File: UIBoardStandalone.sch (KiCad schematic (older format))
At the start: 61 parts, among them J1 Conn_02x08_Odd_Even, J2 Conn_02x15_Odd_Even, SW1 Button_X, SW10 Button_6, SW11 Button_S, SW12 Button_7, SW13 Button_8, SW14 Button_9, SW15 Button_G, SW16 Button_Y, SW17 Button_0, SW18 Button_Z, SW2 Button_R, SW3 Button_1, SW4 Button_2, SW5 Button_3, SW6 Button_P, SW7 Button_M, SW8 Button_4, SW9 Button_5, U1 HD1077R, U10 HD1077R, U11 HD1077R, U12 HD1077R, U13 HD1077R, U14 HD1077R, U15 HD1077R, U16 HD1077R, U17 MM74C923WM, U2 HD1077R, U3 HD1077R, U4 HD1077R, U5 HD1077R, U6 HD1077R, U7 HD1077R, U8 HD1077R, U9 HD1077R

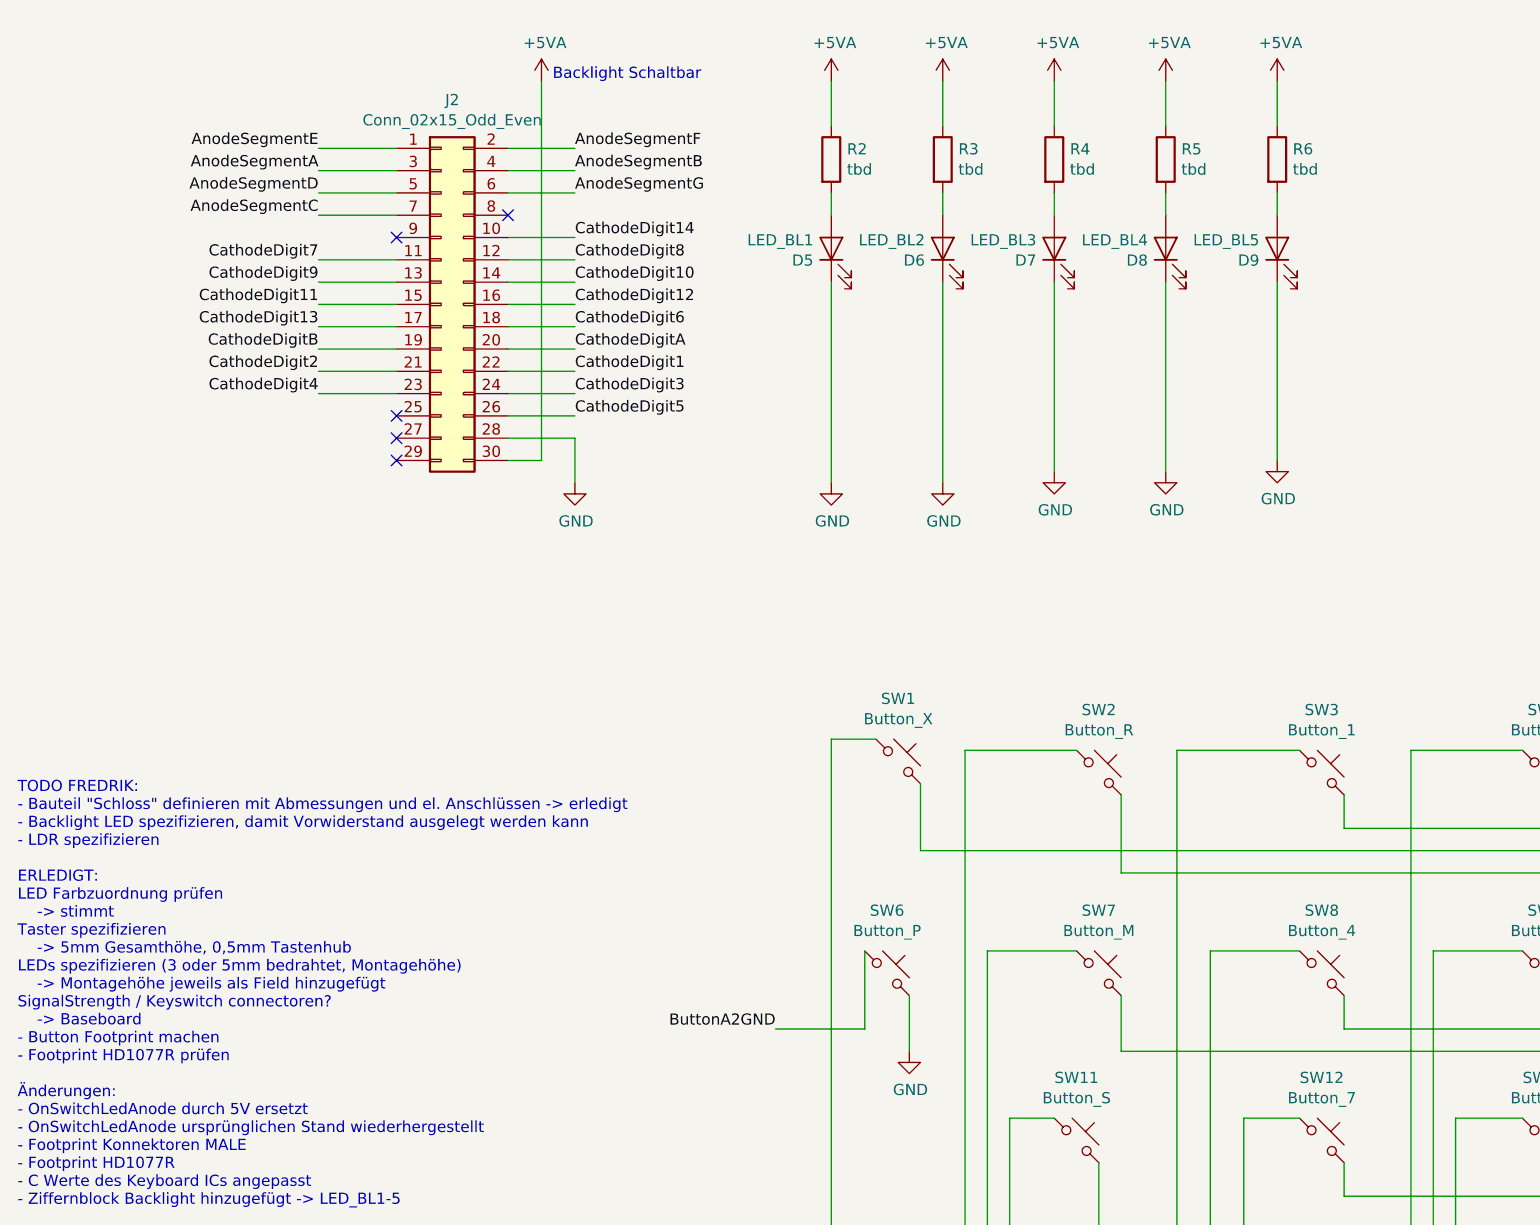
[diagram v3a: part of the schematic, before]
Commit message: - R Values hinzugefügt - Text aktualisiert - vorläufe BOM hinzugefügt
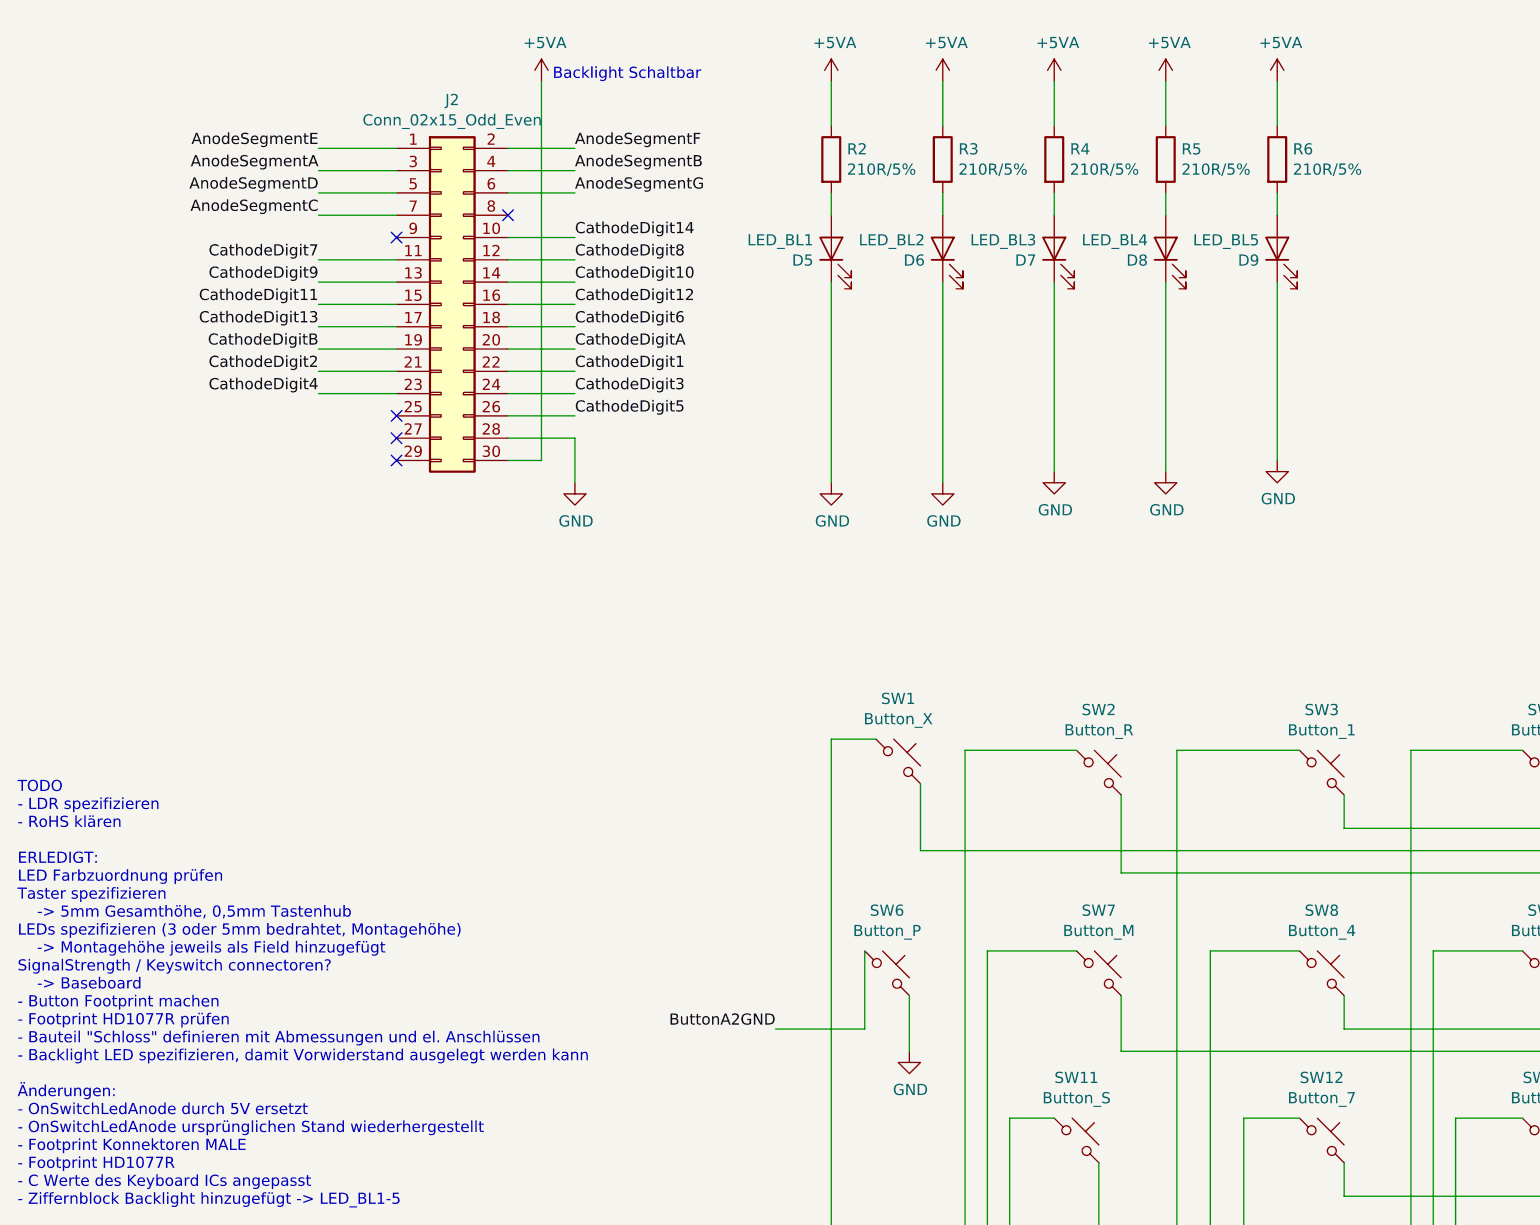
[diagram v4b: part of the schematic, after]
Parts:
- D1, D2, D3: Montagehoehe Lichtes Mass (none) -> 9mm; Montagehöhe 9mm -> (none)
- D4: Montagehoehe Lichtes Mass (none) -> 8mm; Montagehöhe 8mm -> (none)
- D5, D6, D7, D8, D9: Digikey Part Number 1516-QBL7IW60D-WW-ND -> (none); Montagehoehe Lichtes Mass (none) -> 10mm; Montagehöhe 10mm -> (none)
- R1: Montagehoehe Lichtes Mass (none) -> 7mm; Montagehöhe 7mm -> (none)
- R2, R3, R4, R5, R6: value tbd -> 210R/5%
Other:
- note added: "TODO\n- LDR spezifizieren\n- RoHS klären\n\nERLEDIGT:\nLED Farbzuordnung prüfen\nTaster spezifizieren\n -> 5mm Gesamthöhe, 0,5mm Tastenhub\nLEDs spezifizieren (3 oder 5mm bedrahtet, Montagehöhe)\n -> Montagehöhe jeweils als Field hinzugefügt\nSignalStrength / Keyswitch connectoren?\n -> Baseboard\n- Button Footprint machen\n- Footprint HD1077R prüfen\n- Bauteil "Schloss" definieren mit Abmessunge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"
- note removed: "TODO FREDRIK:\n- Bauteil "Schloss" definieren mit Abmessungen und el. Anschlüssen -> erledigt\n- Backlight LED spezifizieren, damit Vorwiderstand ausgelegt werden kann\n- LDR spezifizieren\n\nERLEDIGT:\nLED Farbzuordnung prüfen\n -> stimmt\nTaster spezifizieren\n -> 5mm Gesamthöhe, 0,5mm Tastenhub\nLEDs spezifizieren (3 oder 5mm bedrahtet, Montagehöhe)\n -> Montagehöhe jeweils als Field hinzugefü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"
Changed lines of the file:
@@
 F 1 "LED_RD" V 10788 4330 50  0000 L CNN
 F 2 "LED_THT:LED_D5.0mm" H 10750 4250 50  0001 C CNN
-F 3 "https://www.aopled.com/AOP_PDFs/L513SRD-B.pdf" H 10750 4250 50  0001 C CNN
-F 4 "9mm" V 10750 4250 50  0001 C CNN "Montagehöhe"
+F 3 "" H 10750 4250 50  0001 C CNN
+F 4 "9mm" V 10750 4250 50  0001 C CNN "Montagehoehe Lichtes Mass"
 	1    10750 4250
 	0    -1   -1   0
@@
 F 1 "LED_YL" V 10288 4330 50  0000 L CNN
 F 2 "LED_THT:LED_D5.0mm" H 10250 4250 50  0001 C CNN
-F 3 "https://media.digikey.com/pdf/Data%20Sheets/Lite-On%20PDFs/LTL-4273.pdf" H 10250 4250 50  0001 C CNN
-F 4 "9mm" V 10250 4250 50  0001 C CNN "Montagehöhe"
+F 3 "" H 10250 4250 50  0001 C CNN
+F 4 "9mm" V 10250 4250 50  0001 C CNN "Montagehoehe Lichtes Mass"
 	1    10250 4250
 	0    -1   -1   0
@@
 F 1 "LED_GN" V 9638 4330 50  0000 L CNN
 F 2 "LED_THT:LED_D5.0mm" H 9600 4250 50  0001 C CNN
-F 3 "https://www.aopled.com/AOP_PDFs/L513GD-B.pdf" H 9600 4250 50  0001 C CNN
-F 4 "9mm" V 9600 4250 50  0001 C CNN "Montagehöhe"
+F 3 "" H 9600 4250 50  0001 C CNN
+F 4 "9mm" V 9600 4250 50  0001 C CNN "Montagehoehe Lichtes Mass"
 	1    9600 4250
 	0    -1   -1   0
@@
 F 1 "LED_ON" V 11288 4330 50  0000 L CNN
 F 2 "LED_THT:LED_D3.0mm" H 11250 4250 50  0001 C CNN
-F 3 "https://media.digikey.com/pdf/Data%20Sheets/Lite-On%20PDFs/LTL-1CHYE.pdf" H 11250 4250 50  0001 C CNN
-F 4 "8mm" V 11250 4250 50  0001 C CNN "Montagehöhe"
+F 3 "" H 11250 4250 50  0001 C CNN
+F 4 "8mm" V 11250 4250 50  0001 C CNN "Montagehoehe Lichtes Mass"
 	1    11250 4250
 	0    -1   -1   0
@@
 F 1 "LDR" H 11970 4255 50  0000 L CNN
 F 2 "OptoDevice:R_LDR_4.9x4.2mm_P2.54mm_Vertical" V 11950 4050 50  0001 L CNN
-F 3 "~" H 11900 4250 50  0001 C CNN
-F 4 "7mm" H 11900 4300 50  0001 C CNN "Montagehöhe"
+F 3 "" H 11900 4250 50  0001 C CNN
+F 4 "7mm" H 11900 4300 50  0001 C CNN "Montagehoehe Lichtes Mass"
 	1    11900 4300
 	-1   0    0    1
@@
 LED_GN
 Text Notes 1050 8550 0    50   ~ 0
-TODO FREDRIK:\n- Bauteil "Schloss" definieren mit Abmessungen und el. Anschlüssen -> erledigt\n- Backlight LED spezifizieren, damit Vorwiderstand ausgelegt werden kann\n- LDR spezifizieren\n\nERLEDIGT:\nLED Farbzuordnung prüfen\n    -> stimmt\nTaster spezifizieren\n    -> 5mm Gesamthöhe, 0,5mm Tastenhub\nLEDs spezifizieren (3 oder 5mm bedrahtet, Montagehöhe)\n    -> Montagehöhe jeweils als Field hinzugefügt\nSignalStrength / Keyswitch connectoren?\n    -> Baseboard\n- Button Footprint machen\n- Footprint HD1077R prüfen\n\nÄnderungen:\n- OnSwitchLedAnode durch 5V ersetzt\n- OnSwitchLedAnode ursprünglichen Stand wiederhergestellt\n- Footprint Konnektoren MALE\n- Footprint HD1077R\n- C Werte des Keyboard ICs angepasst\n- Ziffernblock Backlight hinzugefügt -> LED_BL1-5
+TODO\n- LDR spezifizieren\n- RoHS klären\n\nERLEDIGT:\nLED Farbzuordnung prüfen\nTaster spezifizieren\n    -> 5mm Gesamthöhe, 0,5mm Tastenhub\nLEDs spezifizieren (3 oder 5mm bedrahtet, Montagehöhe)\n    -> Montagehöhe jeweils als Field hinzugefügt\nSignalStrength / Keyswitch connectoren?\n    -> Baseboard\n- Button Footprint machen\n- Footprint HD1077R prüfen\n- Bauteil "Schloss" definieren mit Abmessungen und el. Anschlüssen\n- Backlight LED spezifizieren, damit Vorwiderstand ausgelegt werden kann\n\nÄnderungen:\n- OnSwitchLedAnode durch 5V ersetzt\n- OnSwitchLedAnode ursprünglichen Stand wiederhergestellt\n- Footprint Konnektoren MALE\n- Footprint HD1077R\n- C Werte des Keyboard ICs angepasst\n- Ziffernblock Backlight hinzugefügt -> LED_BL1-5
 Wire Wire Line
 	13650 4700 13900 4700
@@
 F 1 "LED_BL1" V 4738 4330 50  0000 L CNN
 F 2 "LED_THT:LED_D3.0mm" H 4700 4250 50  0001 C CNN
-F 3 "http://www.qt-brightek.com/datasheet/QBL7IW60D-XX.pdf" H 4700 4250 50  0001 C CNN
-F 4 "10mm" V 4700 4250 50  0001 C CNN "Montagehöhe"
-F 5 "1516-QBL7IW60D-WW-ND" V 4700 4250 50  0001 C CNN "Digikey Part Number"
+F 3 "" H 4700 4250 50  0001 C CNN
+F 4 "10mm" V 4700 4250 50  0001 C CNN "Montagehoehe Lichtes Mass"
 	1    4700 4250
 	0    -1   -1   0
@@
 F 1 "LED_BL2" V 5238 4330 50  0000 L CNN
 F 2 "LED_THT:LED_D3.0mm" H 5200 4250 50  0001 C CNN
-F 3 "http://www.qt-brightek.com/datasheet/QBL7IW60D-XX.pdf" H 5200 4250 50  0001 C CNN
-F 4 "10mm" V 5200 4250 50  0001 C CNN "Montagehöhe"
-F 5 "1516-QBL7IW60D-WW-ND" V 5200 4250 50  0001 C CNN "Digikey Part Number"
+F 3 "" H 5200 4250 50  0001 C CNN
+F 4 "10mm" V 5200 4250 50  0001 C CNN "Montagehoehe Lichtes Mass"
 	1    5200 4250
 	0    -1   -1   0
@@
 F 1 "LED_BL3" V 5738 4330 50  0000 L CNN
 F 2 "LED_THT:LED_D3.0mm" H 5700 4250 50  0001 C CNN
-F 3 "http://www.qt-brightek.com/datasheet/QBL7IW60D-XX.pdf" H 5700 4250 50  0001 C CNN
-F 4 "10mm" V 5700 4250 50  0001 C CNN "Montagehöhe"
-F 5 "1516-QBL7IW60D-WW-ND" V 5700 4250 50  0001 C CNN "Digikey Part Number"
+F 3 "" H 5700 4250 50  0001 C CNN
+F 4 "10mm" V 5700 4250 50  0001 C CNN "Montagehoehe Lichtes Mass"
 	1    5700 4250
 	0    -1   -1   0
@@
 F 1 "LED_BL4" V 6238 4330 50  0000 L CNN
 F 2 "LED_THT:LED_D3.0mm" H 6200 4250 50  0001 C CNN
-F 3 "http://www.qt-brightek.com/datasheet/QBL7IW60D-XX.pdf" H 6200 4250 50  0001 C CNN
-F 4 "10mm" V 6200 4250 50  0001 C CNN "Montagehöhe"
-F 5 "1516-QBL7IW60D-WW-ND" V 6200 4250 50  0001 C CNN "Digikey Part Number"
+F 3 "" H 6200 4250 50  0001 C CNN
+F 4 "10mm" V 6200 4250 50  0001 C CNN "Montagehoehe Lichtes Mass"
 	1    6200 4250
 	0    -1   -1   0
@@
 F 1 "LED_BL5" V 6738 4330 50  0000 L CNN
 F 2 "LED_THT:LED_D3.0mm" H 6700 4250 50  0001 C CNN
-F 3 "http://www.qt-brightek.com/datasheet/QBL7IW60D-XX.pdf" H 6700 4250 50  0001 C CNN
-F 4 "10mm" V 6700 4250 50  0001 C CNN "Montagehöhe"
-F 5 "1516-QBL7IW60D-WW-ND" V 6700 4250 50  0001 C CNN "Digikey Part Number"
+F 3 "" H 6700 4250 50  0001 C CNN
+F 4 "10mm" V 6700 4250 50  0001 C CNN "Montagehoehe Lichtes Mass"
 	1    6700 4250
 	0    -1   -1   0
@@
 P 4700 3850
 F 0 "R2" H 4770 3896 50  0000 L CNN
-F 1 "tbd" H 4770 3805 50  0000 L CNN
+F 1 "210R/5%" H 4770 3805 50  0000 L CNN
 F 2 "Resistor_SMD:R_0603_1608Metric" V 4630 3850 50  0001 C CNN
 F 3 "~" H 4700 3850 50  0001 C CNN
@@
 P 5200 3850
 F 0 "R3" H 5270 3896 50  0000 L CNN
-F 1 "tbd" H 5270 3805 50  0000 L CNN
+F 1 "210R/5%" H 5270 3805 50  0000 L CNN
 F 2 "Resistor_SMD:R_0603_1608Metric" V 5130 3850 50  0001 C CNN
 F 3 "~" H 5200 3850 50  0001 C CNN
@@
 P 5700 3850
 F 0 "R4" H 5770 3896 50  0000 L CNN
-F 1 "tbd" H 5770 3805 50  0000 L CNN
+F 1 "210R/5%" H 5770 3805 50  0000 L CNN
 F 2 "Resistor_SMD:R_0603_1608Metric" V 5630 3850 50  0001 C CNN
 F 3 "~" H 5700 3850 50  0001 C CNN
@@
 P 6200 3850
 F 0 "R5" H 6270 3896 50  0000 L CNN
-F 1 "tbd" H 6270 3805 50  0000 L CNN
+F 1 "210R/5%" H 6270 3805 50  0000 L CNN
 F 2 "Resistor_SMD:R_0603_1608Metric" V 6130 3850 50  0001 C CNN
 F 3 "~" H 6200 3850 50  0001 C CNN
@@
 P 6700 3850
 F 0 "R6" H 6770 3896 50  0000 L CNN
-F 1 "tbd" H 6770 3805 50  0000 L CNN
+F 1 "210R/5%" H 6770 3805 50  0000 L CNN
 F 2 "Resistor_SMD:R_0603_1608Metric" V 6630 3850 50  0001 C CNN
 F 3 "~" H 6700 3850 50  0001 C CNN

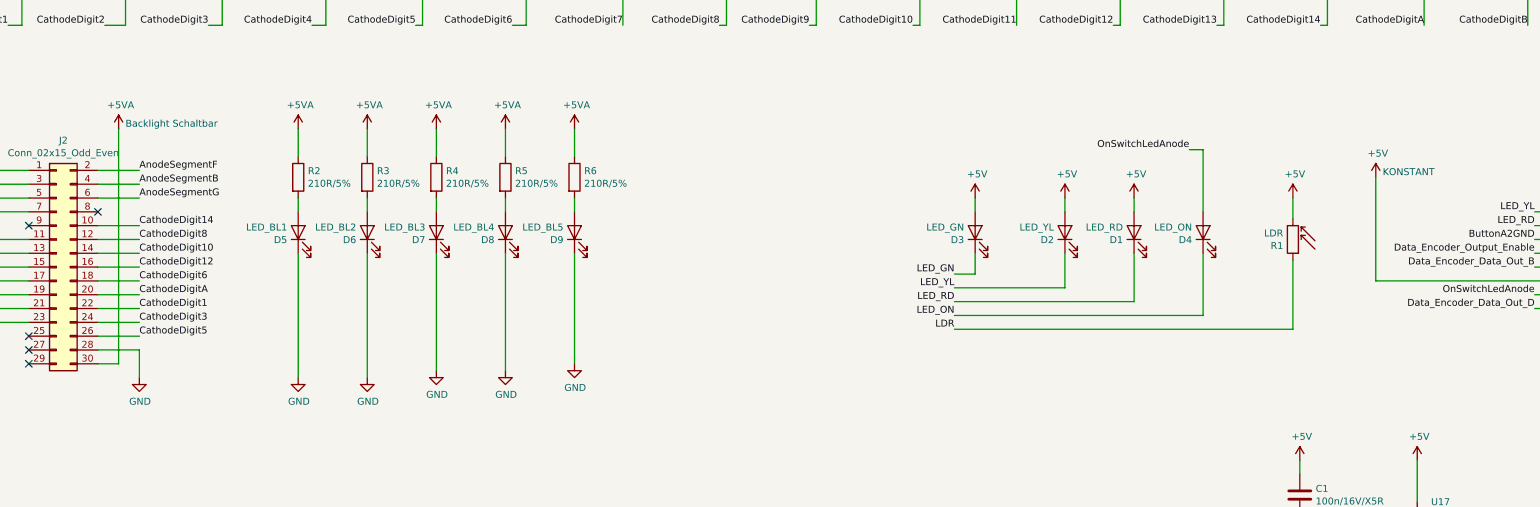
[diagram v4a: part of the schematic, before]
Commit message: - UI Backlight schaltbar gemacht, erster Entwurf, +5VA Symbol durch Label ersetzt
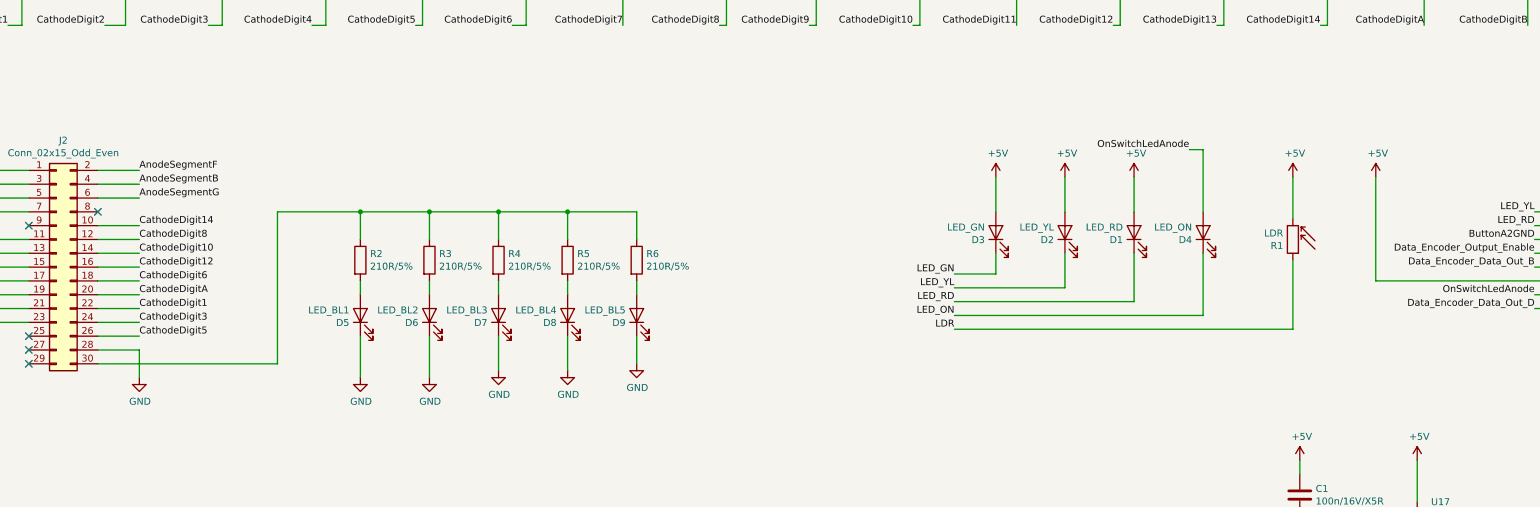
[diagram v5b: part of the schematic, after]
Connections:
- net +5VA: no longer names the net of J2.30 (Pin_30), R2.1, R3.1, R4.1, R5.1, R6.1
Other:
- note removed: "Backlight Schaltbar"
- note removed: "KONSTANT\n"
- moved on the sheet: D3, D5, D6, D7, D8, D9, R2, R3, R4, R5, R6
